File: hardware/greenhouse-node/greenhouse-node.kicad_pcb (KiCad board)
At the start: 2 copper layers, 90.2 x 69.8 mm, 43 parts, among them J1 Conn_01x04_Male, J2 Conn_01x12_Male, J3 Conn_01x02_Male, J4 Conn_01x02_Male, J5 RX_PinHeader_1x04_P2.54mm, J6 TX_PinHeader_1x04_P2.54mm, J7 Conn_01x02_Male, Q1 BC549C, Q2 BC549C, Q3 IRF9530N, Q4 IRF530N, Q6 IRF9530N, Q7 IRF530N, Q8 BC549C, U1 ATtiny84A-P, U2 L7805, U3 74HC595

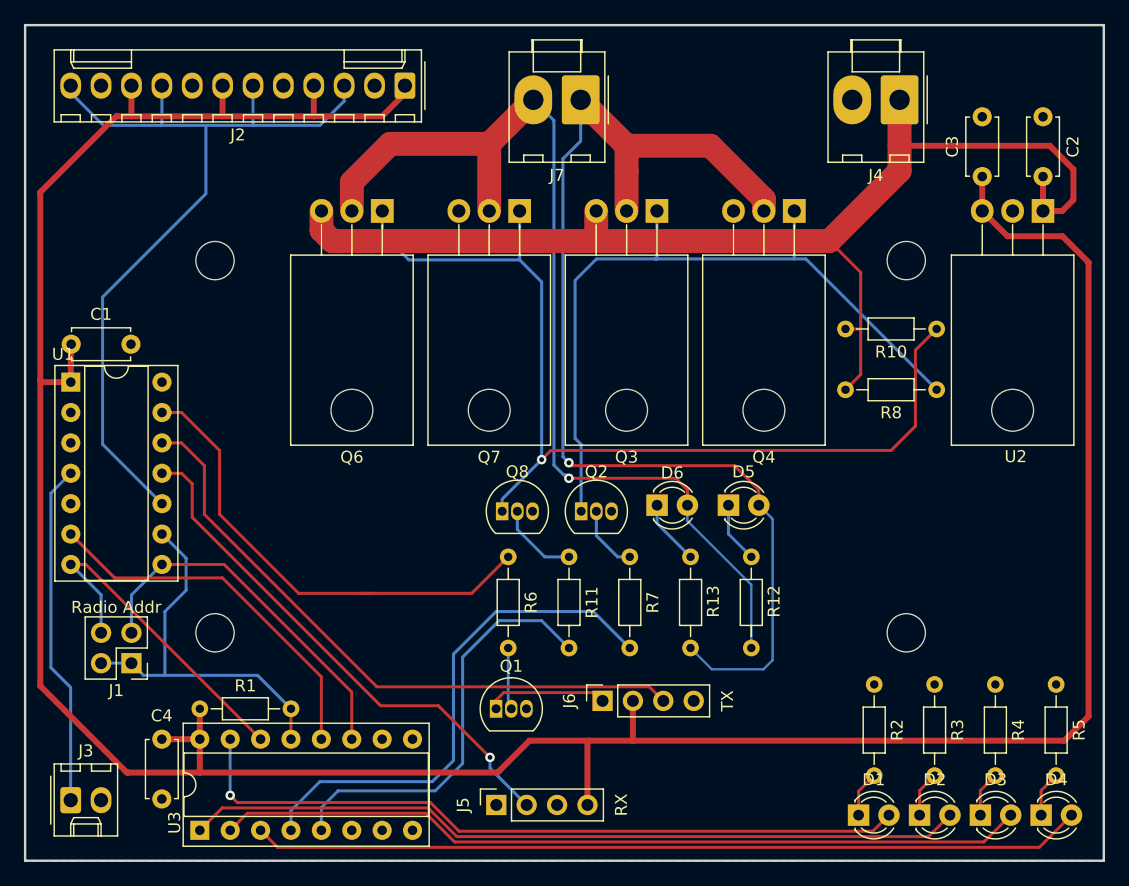
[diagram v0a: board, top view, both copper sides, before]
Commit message: Make H-bridge PWM enabled
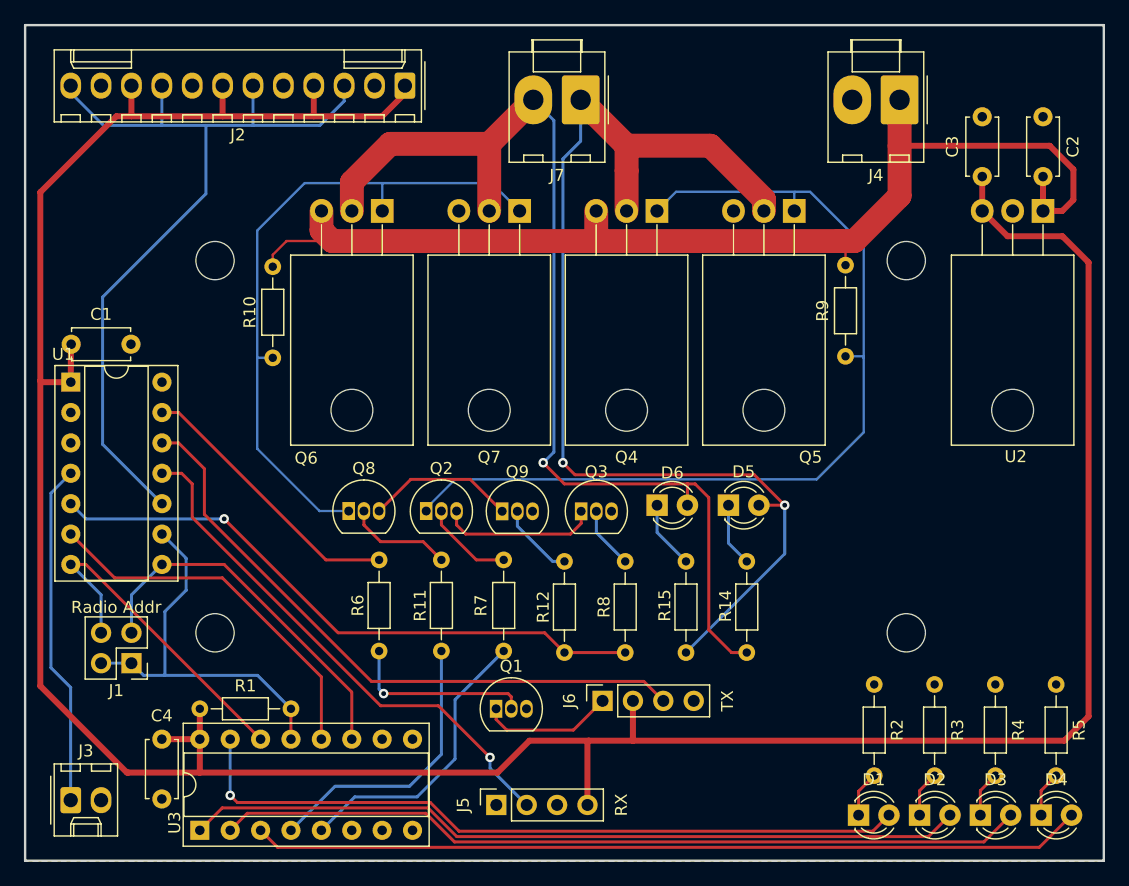
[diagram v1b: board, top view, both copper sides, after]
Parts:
- added Q2: BC549C, Package_TO_SOT_THT:TO-92_Inline, F.Cu at (161.8, 86.3)
- added Q8: BC549C, Package_TO_SOT_THT:TO-92_Inline, F.Cu at (155.3, 86.3)
- added R11: 1k, Resistor_THT:R_Axial_DIN0204_L3.6mm_D1.6mm_P7.62mm_Horizontal, F.Cu at (163.1, 90.4)
- added R7: 1k, Resistor_THT:R_Axial_DIN0204_L3.6mm_D1.6mm_P7.62mm_Horizontal, F.Cu at (168.3, 90.4)
- R10: value 10k -> 2k
- R9: renamed from R8; value 10k -> 2k
- moved R10 55.6 mm to (149.0, 73.5), turned to 90 degrees
- moved R6 10.8 mm to (157.9, 98.0)
- moved R9 8.12 mm to (196.8, 73.4), turned to 90 degrees
- moved R12 0.54 mm to (173.4, 90.6)
- moved R14 0.54 mm to (188.6, 98.2)
- moved R15 0.54 mm to (183.5, 98.2)
- moved R8 0.54 mm to (178.4, 90.6)
- renumbered Q2 to Q3, Q3 to Q4, Q4 to Q5, Q8 to Q9, R11 to R12, R12 to R14, R13 to R15, R7 to R8
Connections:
- Q3 pad 1: Net-(Q2-Pad1) -> Net-(Q2-Pad3)
- Q9 pad 1: Net-(Q6-Pad1) -> Net-(Q8-Pad3)
- R12 pad 2: Motor_B -> Motor_PWM
- R8 pad 2: Motor_A -> Motor_PWM
- U1 pad 5: unconnected-(U1-Pad5) -> Motor_PWM
- U3 pad 4: Motor_A -> Motor_B
- U3 pad 5: Motor_B -> Motor_A
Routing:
- net Motor_PWM: track 0.00 -> 51.5 mm, vias 0 -> 1
- net Net-(Q6-Pad1): track 82.8 -> 56.2 mm, vias 1 -> 0
- net Motor_A: track 43.3 -> 24.3 mm
- net /RAD_TX_EN: track 40.4 -> 23.3 mm
- net Net-(Q2-Pad1): track 63.3 -> 78.1 mm
- net Net-(Q2-Pad3): track 0.00 -> 13.3 mm
- net Net-(Q8-Pad3): track 0.00 -> 12.5 mm
- net Motor_B: track 35.2 -> 23.8 mm
- net Net-(Q1-Pad2): track 5.19 -> 15.9 mm, vias 0 -> 1
- net Net-(Q8-Pad2): track 0.00 -> 8.85 mm
- net Net-(Q2-Pad2): track 0.00 -> 7.58 mm
- net +10V: track 100.3 -> 94.9 mm
- net /motor/Motor_2: track 84.7 -> 89.3 mm
- net Net-(J6-Pad1): track 9.19 -> 11.2 mm
- net /motor/Motor_1: track 95.8 -> 94.1 mm, vias 1 -> 2

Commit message: Add pull downs to SR SER+CLK
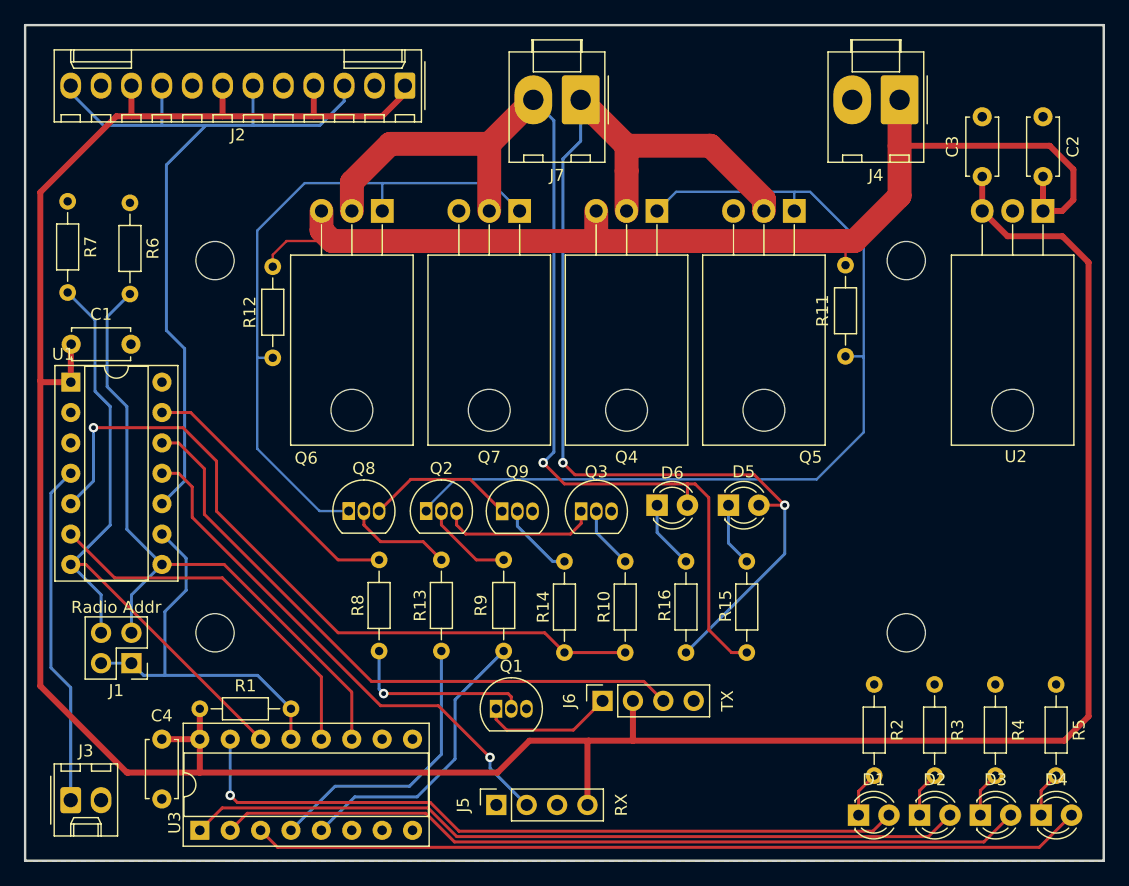
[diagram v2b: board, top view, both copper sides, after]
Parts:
- added R6: 10k, Resistor_THT:R_Axial_DIN0204_L3.6mm_D1.6mm_P7.62mm_Horizontal, F.Cu at (137.0, 60.6)
- added R7: 10k, Resistor_THT:R_Axial_DIN0204_L3.6mm_D1.6mm_P7.62mm_Horizontal, F.Cu at (131.8, 60.5)
- renumbered R8 to R10, R9 to R11, R10 to R12, R11 to R13, R12 to R14, R14 to R15, R15 to R16, R6 to R8, R7 to R9
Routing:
- net /SR_SER: track 28.7 -> 54.2 mm
- net /SR_CLK: track 31.0 -> 56.3 mm
- net Motor_PWM: track 51.5 -> 61.8 mm
- net /OneWire: track 70.0 -> 67.2 mm

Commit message: Remove address pins
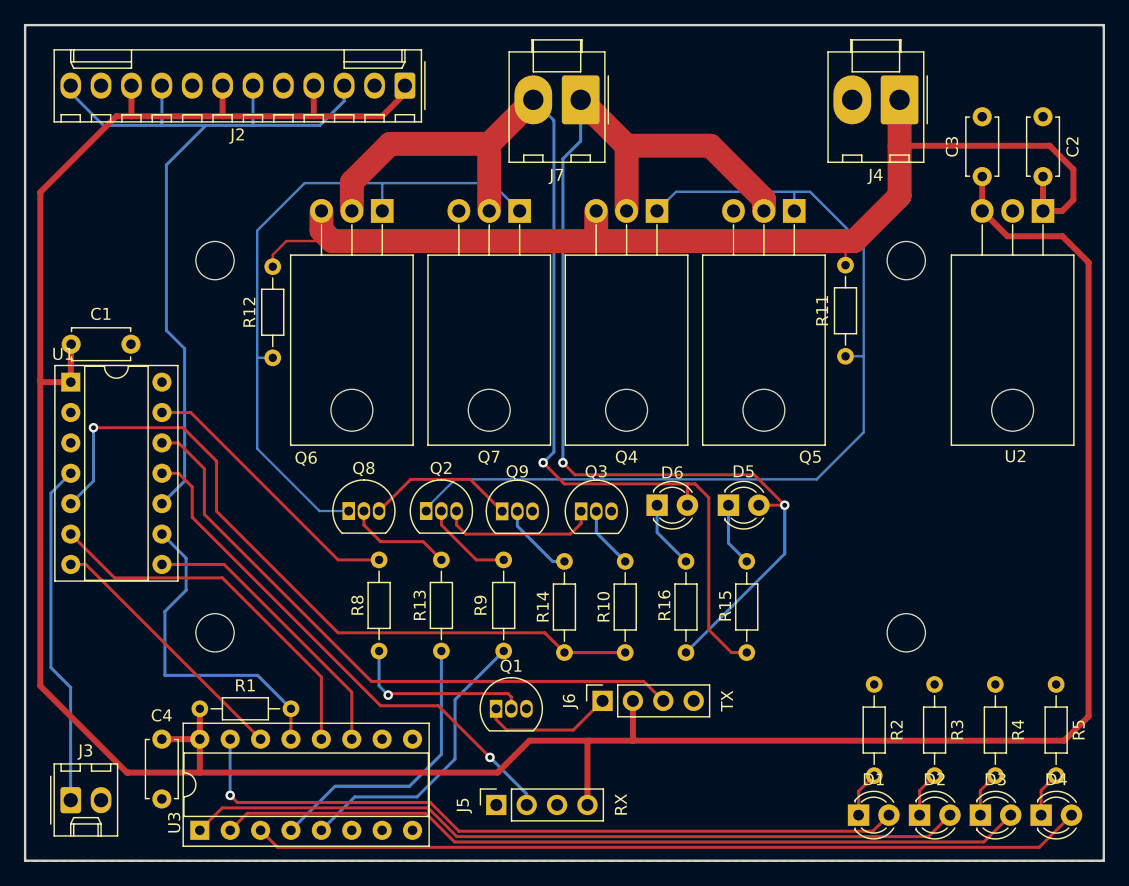
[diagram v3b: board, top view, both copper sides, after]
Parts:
- removed J1: Conn_01x04_Male, Connector_PinHeader_2.54mm:PinHeader_2x02_P2.54mm_Vertical
- removed R6, R7: 10k, Resistor_THT:R_Axial_DIN0204_L3.6mm_D1.6mm_P7.62mm_Horizontal
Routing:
- net /SR_SER: track 54.2 -> 21.9 mm
- net /SR_CLK: track 56.3 -> 24.2 mm
- net /SR_OE: track 33.4 -> 27.6 mm

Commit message: Micro programming connector
Also:
- Connect SRCLR to +5V
- Move 10V pull-up away from micro
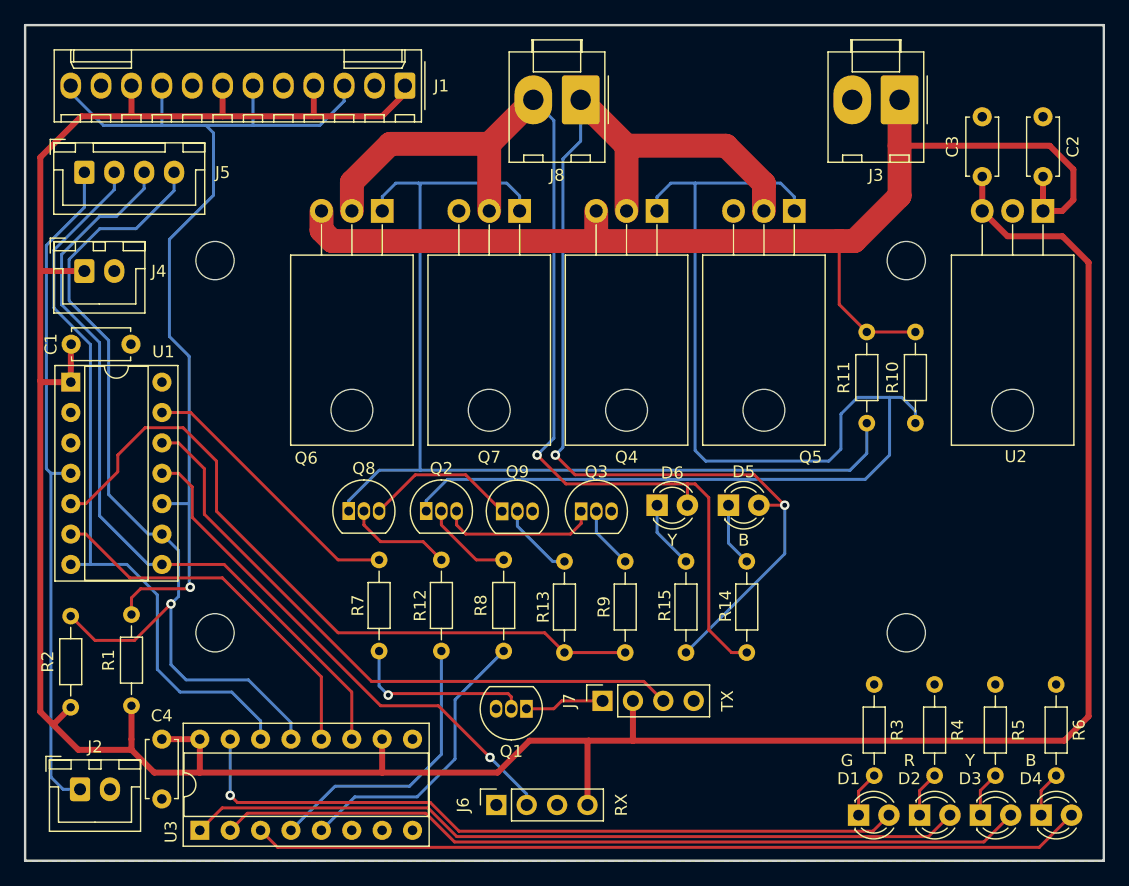
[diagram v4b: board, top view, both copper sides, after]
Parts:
- added J4: Conn_01x02_Male, Connector_JST:JST_XH_B2B-XH-A_1x02_P2.50mm_Vertical, F.Cu at (133.2, 66.3)
- added J5: Conn_01x04_Male, Connector_JST:JST_XH_B4B-XH-A_1x04_P2.50mm_Vertical, F.Cu at (133.2, 58.0)
- added R1: 5k, Resistor_THT:R_Axial_DIN0204_L3.6mm_D1.6mm_P7.62mm_Horizontal, F.Cu at (137.2, 102.6)
- D1: value LED_Small -> LED_Sm_G
- D2: value LED_Small -> LED_Sm_R
- D3: value LED_Small -> LED_Sm_Y
- D4: value LED_Small -> LED_Sm_B
- J2: renamed from J3; footprint Connector_Molex:Molex_KK-254_AE-6410-02A_1x02_P2.54mm_Vertical -> Connector_JST:JST_XH_B2B-XH-A_1x02_P2.50mm_Vertical
- R4: renamed from R3; value 5k -> 1k
- R5: renamed from R4; value 5k -> 1k
- moved R11 50.0 mm to (198.6, 79.0)
- moved R2 10.8 mm to (132.1, 102.7), turned to 90 degrees
- moved R10 8.08 mm to (202.7, 79.0)
- moved Q1 2.54 mm to (170.2, 102.9), turned to 180 degrees
- moved J2 1.20 mm to (132.9, 109.6)
- renumbered J2 to J1, J4 to J3, J5 to J6, J6 to J7, J7 to J8, R11 to R10, R12 to R11, R13 to R12, R14 to R13, R15 to R14, R16 to R15, R1 to R2, R2 to R3, R5 to R6, R8 to R7, R9 to R8, R10 to R9
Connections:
- U3 pad 10: unconnected-(U3-Pad10) -> +5V
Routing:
- net /SR_OE: track 27.6 -> 75.2 mm, vias 0 -> 1
- net /SR_SER: track 21.9 -> 62.6 mm
- net /SR_CLK: track 24.2 -> 64.8 mm
- net Net-(Q6-Pad1): track 56.2 -> 87.1 mm
- net Net-(Q2-Pad1): track 77.8 -> 107.3 mm
- net /Reset: track 28.7 -> 56.6 mm
- net /OneWire: track 67.2 -> 82.8 mm, vias 0 -> 1
- net +5V: track 249.9 -> 262.5 mm
- net +10V: track 94.9 -> 99.6 mm
- net Net-(J7-Pad1): track 11.2 -> 6.63 mm
- net Motor_PWM: track 61.8 -> 60.0 mm, vias 1 -> 0
- net /motor/Motor_1: track 94.1 -> 95.3 mm

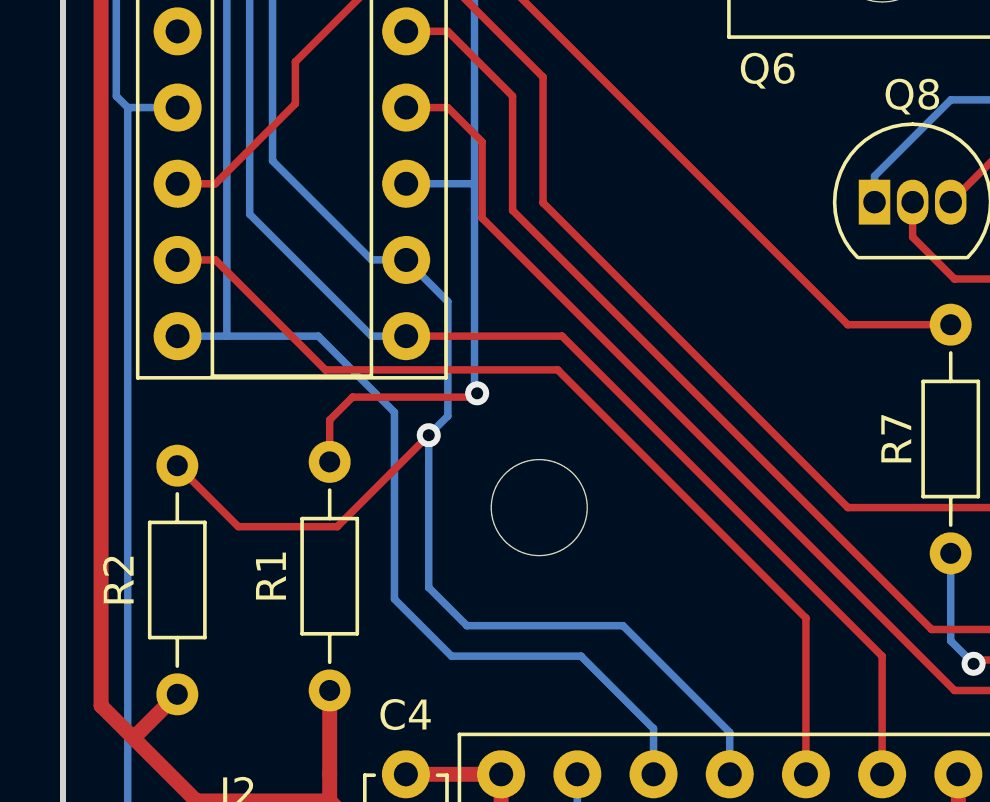
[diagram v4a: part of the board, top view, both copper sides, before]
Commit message: Swap OE and RCLK
Drive OE low
Fixed missing SRCLR pull-up
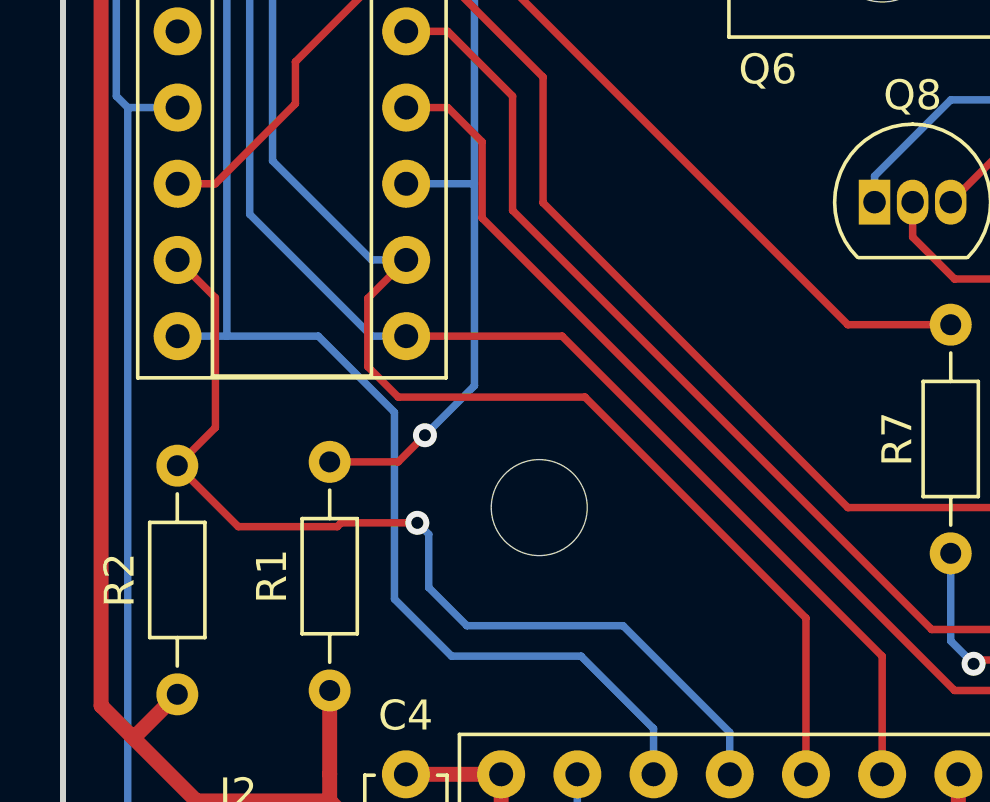
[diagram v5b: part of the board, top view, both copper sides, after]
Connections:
- J5 pad 4: /SR_OE -> /SR_RCLK
- U1 pad 6: /SR_RCLK -> /SR_OE
- U1 pad 9: /SR_OE -> /SR_RCLK
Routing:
- net /SR_OE: track 75.2 -> 32.5 mm
- net /SR_RCLK: track 31.1 -> 66.9 mm
- net /OneWire: track 82.8 -> 81.8 mm
